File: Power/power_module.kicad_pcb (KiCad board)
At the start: 4 copper layers, 198 x 88 mm, 54 parts, among them J1 Conn_02x03_Odd_Even, J10 Conn_01x04, J11 Conn_02x02_Odd_Even, J2 Conn_02x03_Odd_Even, J3 Conn_02x06_Counter_Clockwise, J4 Conn_02x05_Top_Bottom, J5 Conn_02x05_Top_Bottom, J6 Conn_02x02_Odd_Even, J7 Conn_02x02_Odd_Even, J8 Conn_01x06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

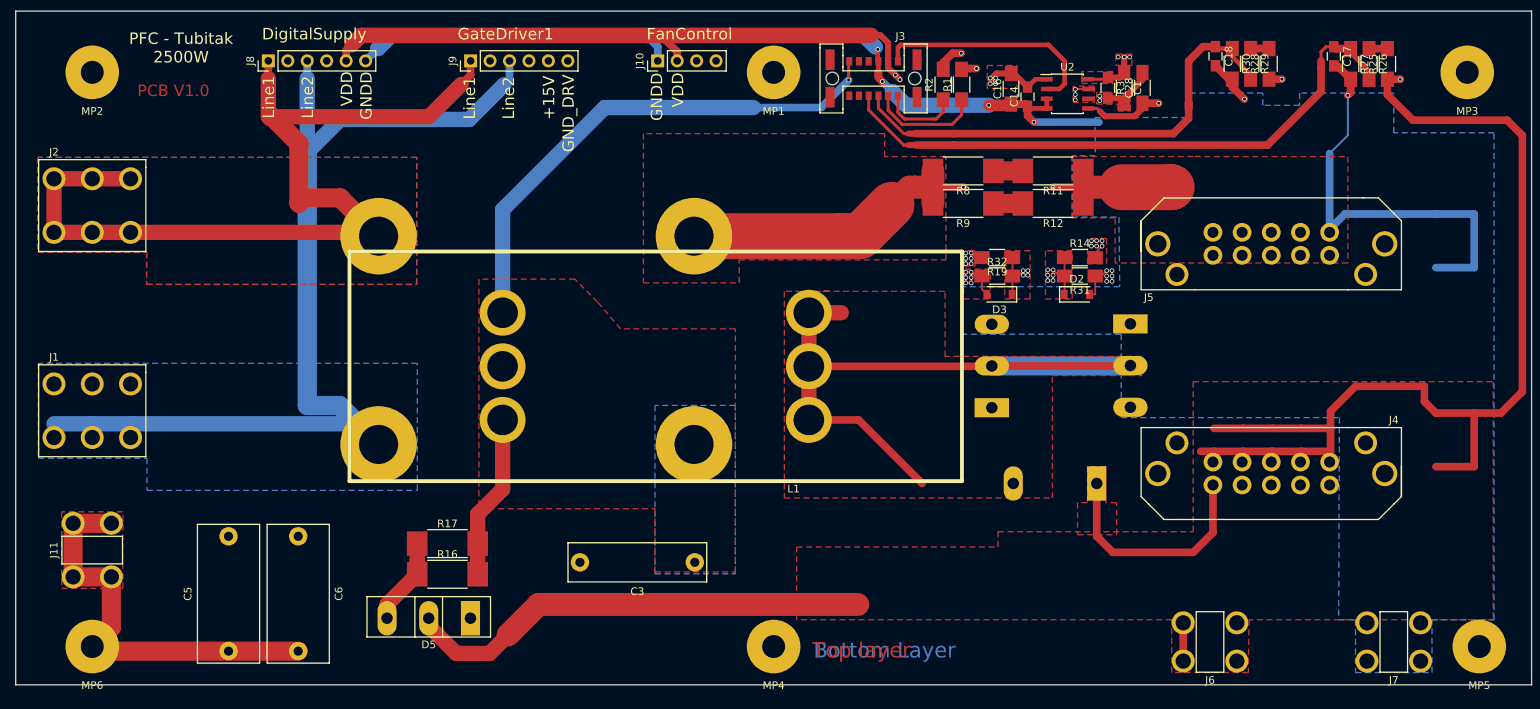
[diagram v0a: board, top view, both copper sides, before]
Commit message: Yuksek akim tasiyan hatlara Mask atildi dolayisiyla bu hatlara lehim takviyesi yapilabilir.
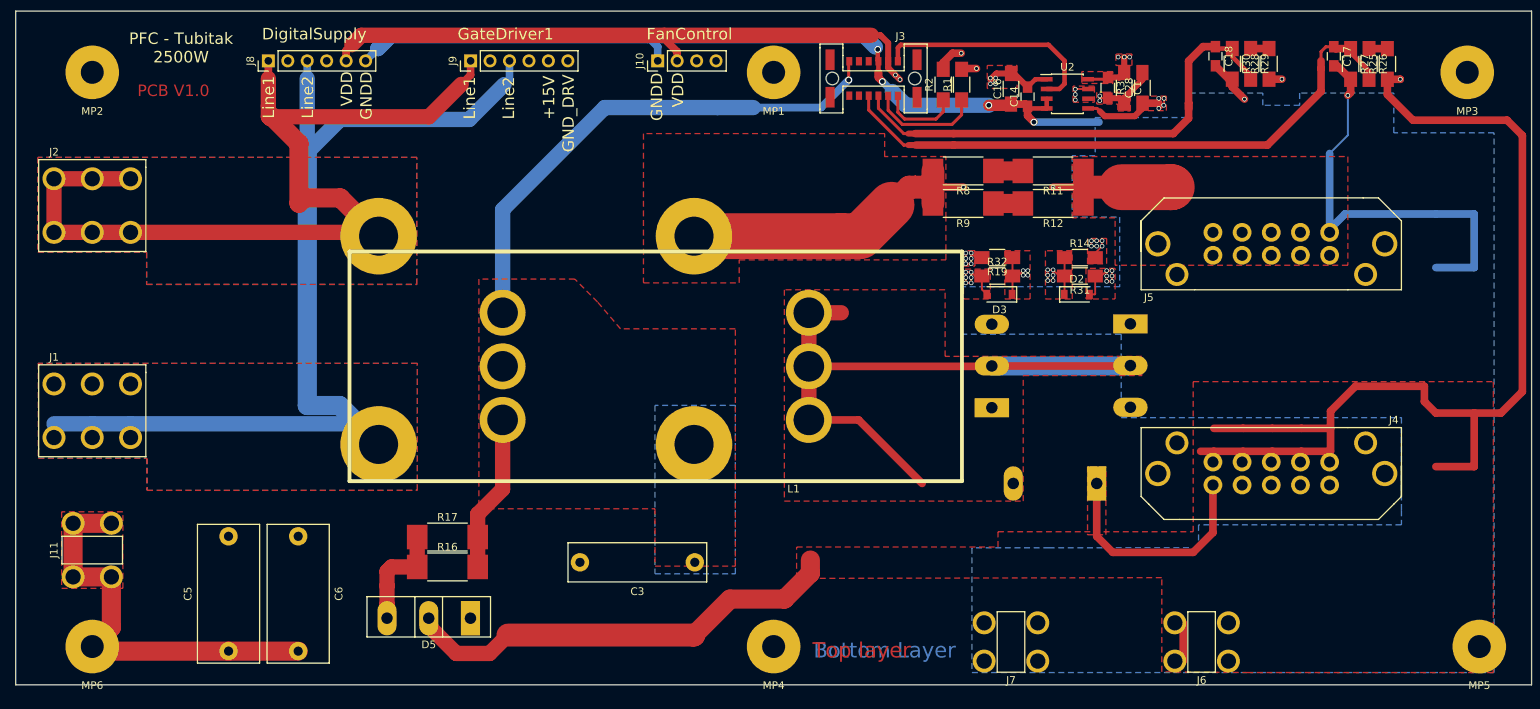
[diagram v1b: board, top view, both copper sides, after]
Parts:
- moved J7 50.0 mm to (230.0, 152.0)
- moved J6 1.10 mm to (254.9, 152.0)
- moved R16 0.96 mm to (156.4, 142.2)
- moved R17 0.86 mm to (156.4, 138.3)
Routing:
- net Net-(D5-Pad3): track 11.4 -> 16.0 mm
- net /15V/1: track 98.1 -> 101.8 mm, vias 1 -> 4
- net /Vout+: track 252.2 -> 249.5 mm
- net GNDA: track 255.6 -> 256.3 mm
- added copper zone on F.Cu, net /15V/1
- added copper zone on F.Cu, net /Line2
- removed copper zone on In2.Cu, net /Line1
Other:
- net class GNDA: clearance 3 -> 0.3

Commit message: Silk katmani duzenlendi. Gerber dosyalari uretildi.
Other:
- board text added: "Gerber üretmek için: http://support.seeedstudio.com/knowledgebase/articles/1824574-how-to-generate-gerber-and-drill-files-from-kicad"
